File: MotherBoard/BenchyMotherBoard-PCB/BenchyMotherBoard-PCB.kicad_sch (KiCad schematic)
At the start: 0 parts

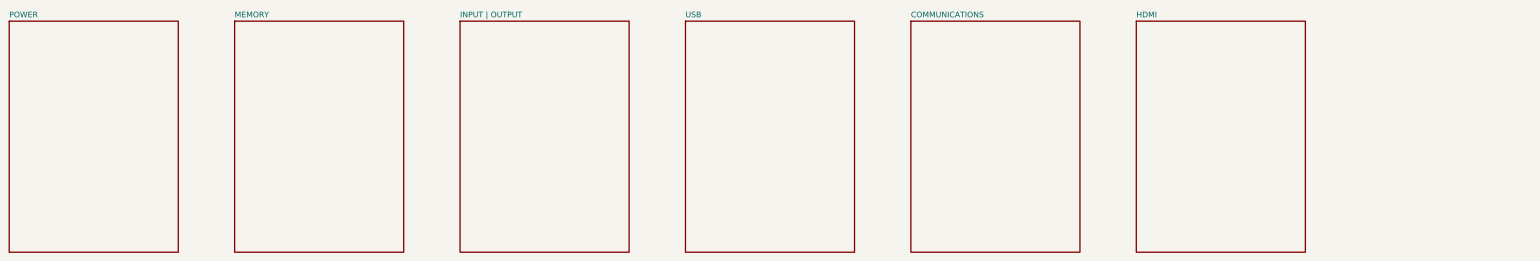
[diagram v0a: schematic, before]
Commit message: Add MORE regulators, USB, Display, and SDCard
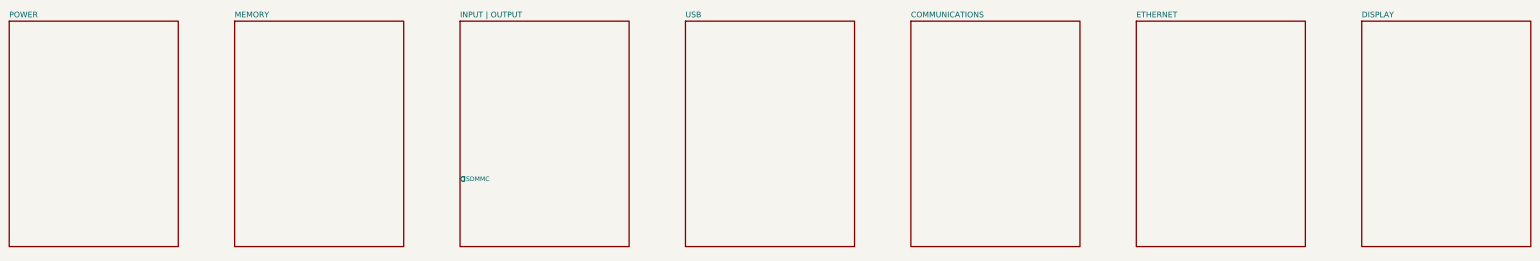
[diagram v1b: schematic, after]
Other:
- sheet HDMI renamed ETHERNET
- added sheet DISPLAY (display.kicad_sch)
- sheet ETHERNET: file hdmi.kicad_sch -> ethernet.kicad_sch
- sheet INPUT | OUTPUT ports: added SDMMC; removed none

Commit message: Initial schematic lock
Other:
- sheet USB renamed USB | DISPLAY
- removed sheet DISPLAY
- removed sheet ETHERNET
- sheet COMMUNICATIONS ports: added COMMS{PWR-SDA PWR-SCK ELOAD-SDA ELOAD-SCK RELAY-SDA RELAY-SCK LOGIC-SDA LOGIC-SCK MAINS-1 MAINS-2 MAINS-3 MAINS-4 MAINS-5 MAINS-6}; removed none
- sheet INPUT | OUTPUT ports: added COMMS{PWR-SDA PWR-SCK ELOAD-SDA ELOAD-SCK RELAY-SDA RELAY-SCK LOGIC-SDA LOGIC-SCK MAINS-1 MAINS-2 MAINS-3 MAINS-4 MAINS-5 MAINS-6}, DISP-USB-BUS{TE BRIGHT USB-RESET USB-SDA USB-SCK}, PWR-BUS{RX TX}; removed SDMMC
- sheet POWER ports: added PWR-BUS{RX TX}; removed none
- sheet USB | DISPLAY ports: added DISP-USB-BUS{TE BRIGHT USB-RESET USB-SDA USB-SCK}; removed none

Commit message: (WIP) Start layout
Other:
- title: Benchy Version 2 -> Benchy Reloaded

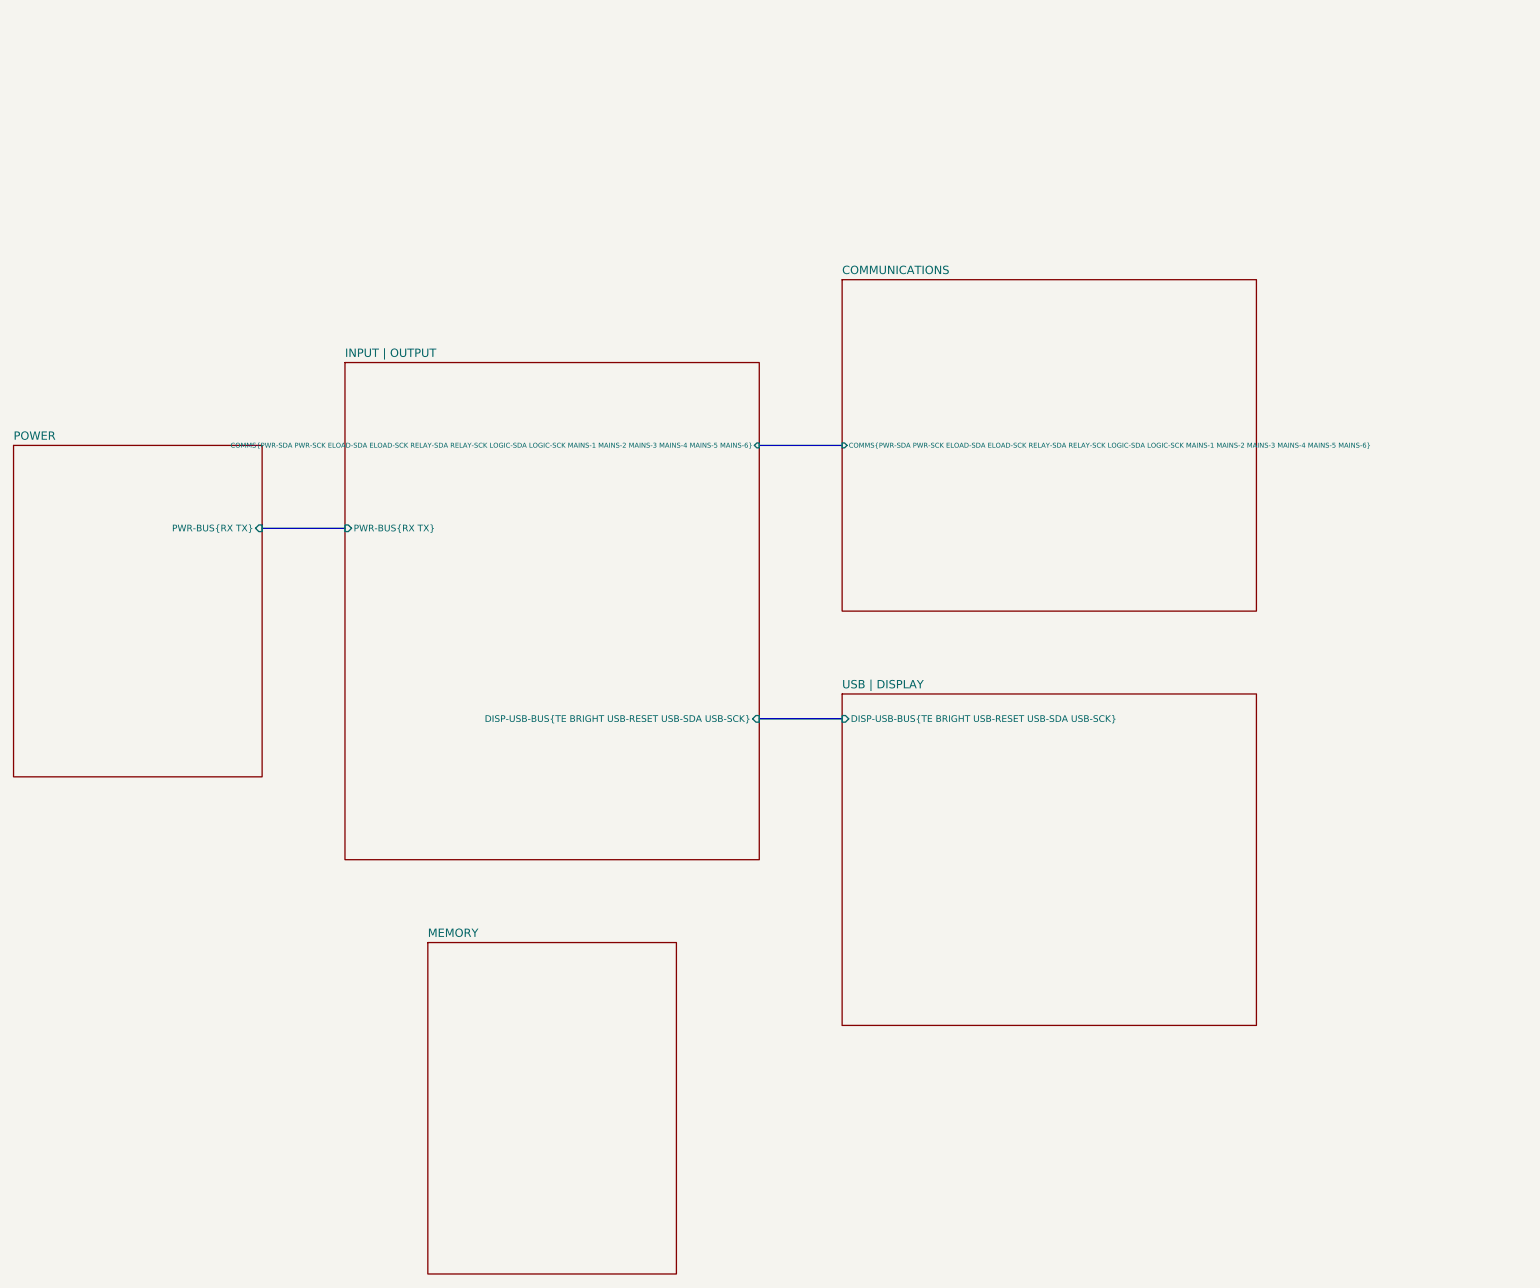
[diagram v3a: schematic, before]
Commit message: (WIP) Replaced DDR VRef with reg and started layout
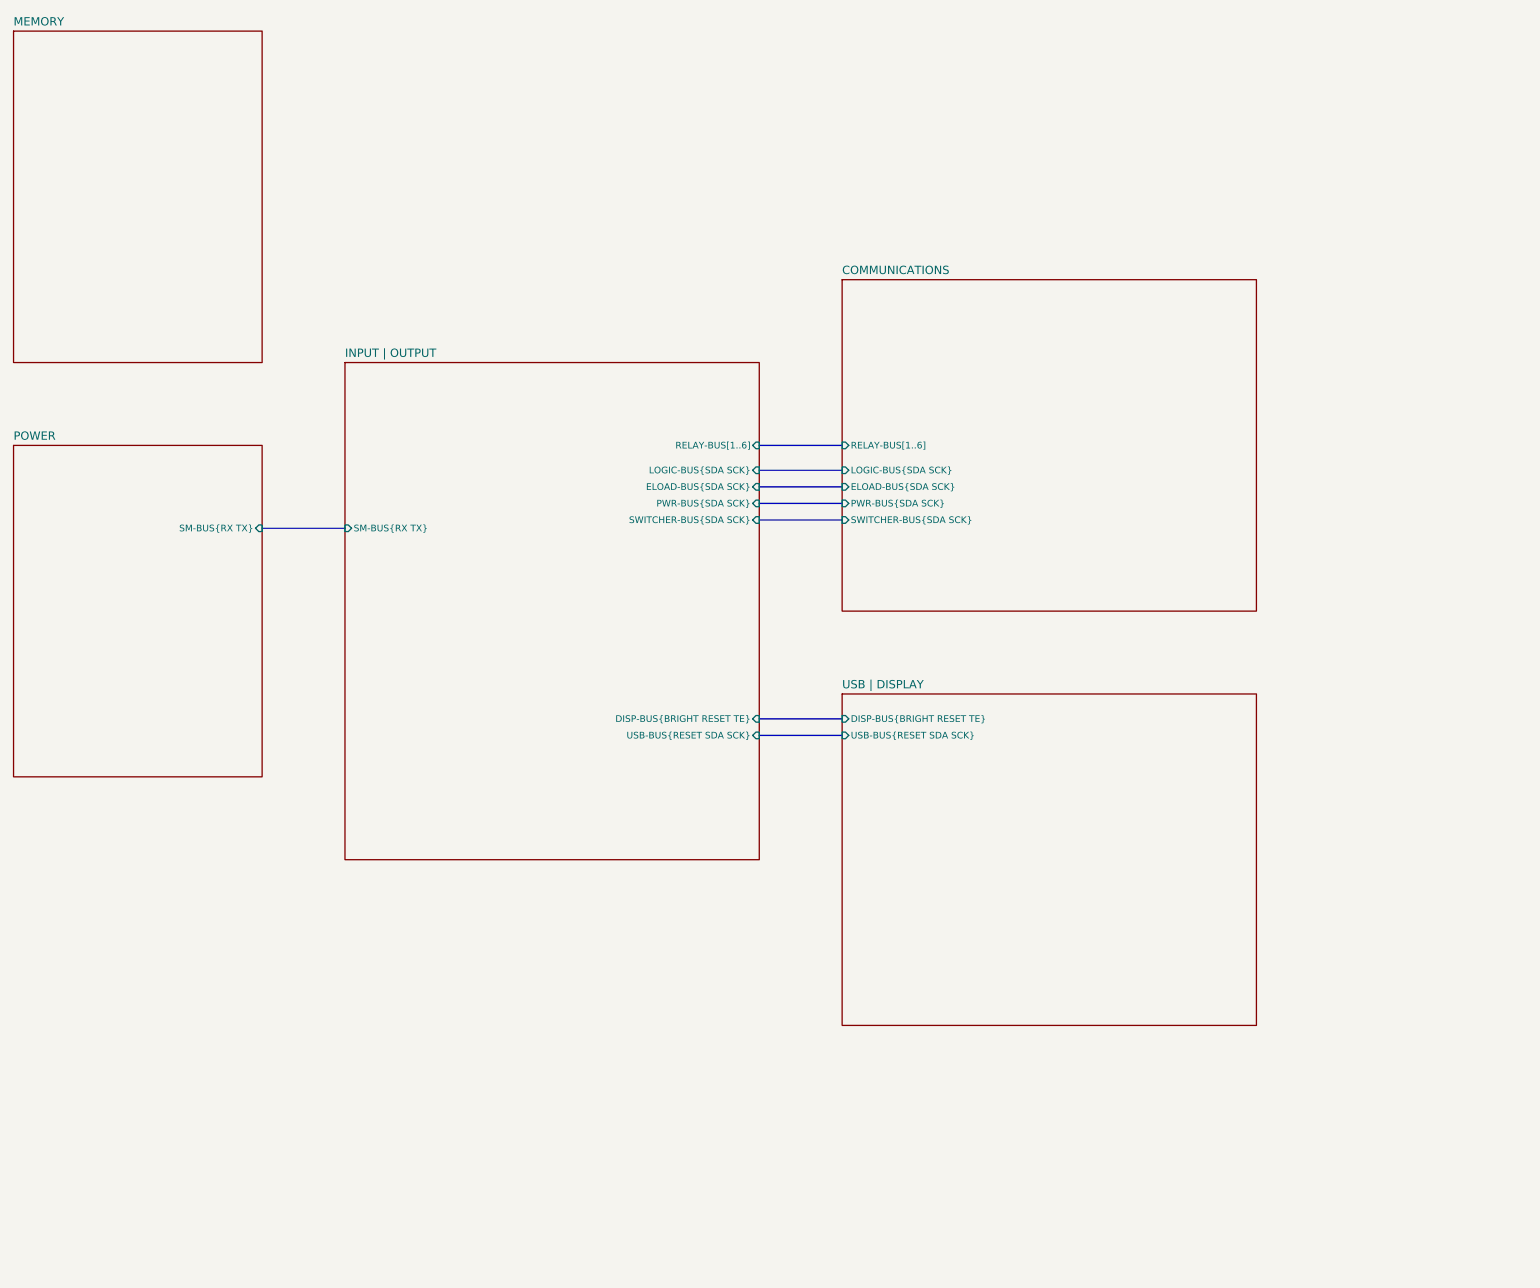
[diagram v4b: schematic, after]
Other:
- sheet COMMUNICATIONS ports: added ELOAD-BUS{SDA SCK}, LOGIC-BUS{SDA SCK}, PWR-BUS{SDA SCK}, RELAY-BUS[1..6], SWITCHER-BUS{SDA SCK}; removed COMMS{PWR-SDA PWR-SCK ELOAD-SDA ELOAD-SCK RELAY-SDA RELAY-SCK LOGIC-SDA LOGIC-SCK MAINS-1 MAINS-2 MAINS-3 MAINS-4 MAINS-5 MAINS-6}
- sheet INPUT | OUTPUT ports: added DISP-BUS{BRIGHT RESET TE}, ELOAD-BUS{SDA SCK}, LOGIC-BUS{SDA SCK}, PWR-BUS{SDA SCK}, RELAY-BUS[1..6], SM-BUS{RX TX}, SWITCHER-BUS{SDA SCK}, USB-BUS{RESET SDA SCK}; removed COMMS{PWR-SDA PWR-SCK ELOAD-SDA ELOAD-SCK RELAY-SDA RELAY-SCK LOGIC-SDA LOGIC-SCK MAINS-1 MAINS-2 MAINS-3 MAINS-4 MAINS-5 MAINS-6}, DISP-USB-BUS{TE BRIGHT USB-RESET USB-SDA USB-SCK}, PWR-BUS{RX TX}
- sheet POWER ports: added SM-BUS{RX TX}; removed PWR-BUS{RX TX}
- sheet USB | DISPLAY ports: added DISP-BUS{BRIGHT RESET TE}, USB-BUS{RESET SDA SCK}; removed DISP-USB-BUS{TE BRIGHT USB-RESET USB-SDA USB-SCK}
